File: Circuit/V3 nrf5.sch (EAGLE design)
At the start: 63 parts, among them J12 AMP FCI 10103594-0001LF, J7 CORTEX_DEBUG_SMD, Q1 BSS138, U1 AL8805, U2 MCP73831, U3 BC840M, U4 3.3V/150mA, U5 AL8805, U6 AL8805, U9 RICHTEK_TECHNOLOGY_CORPORATIO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

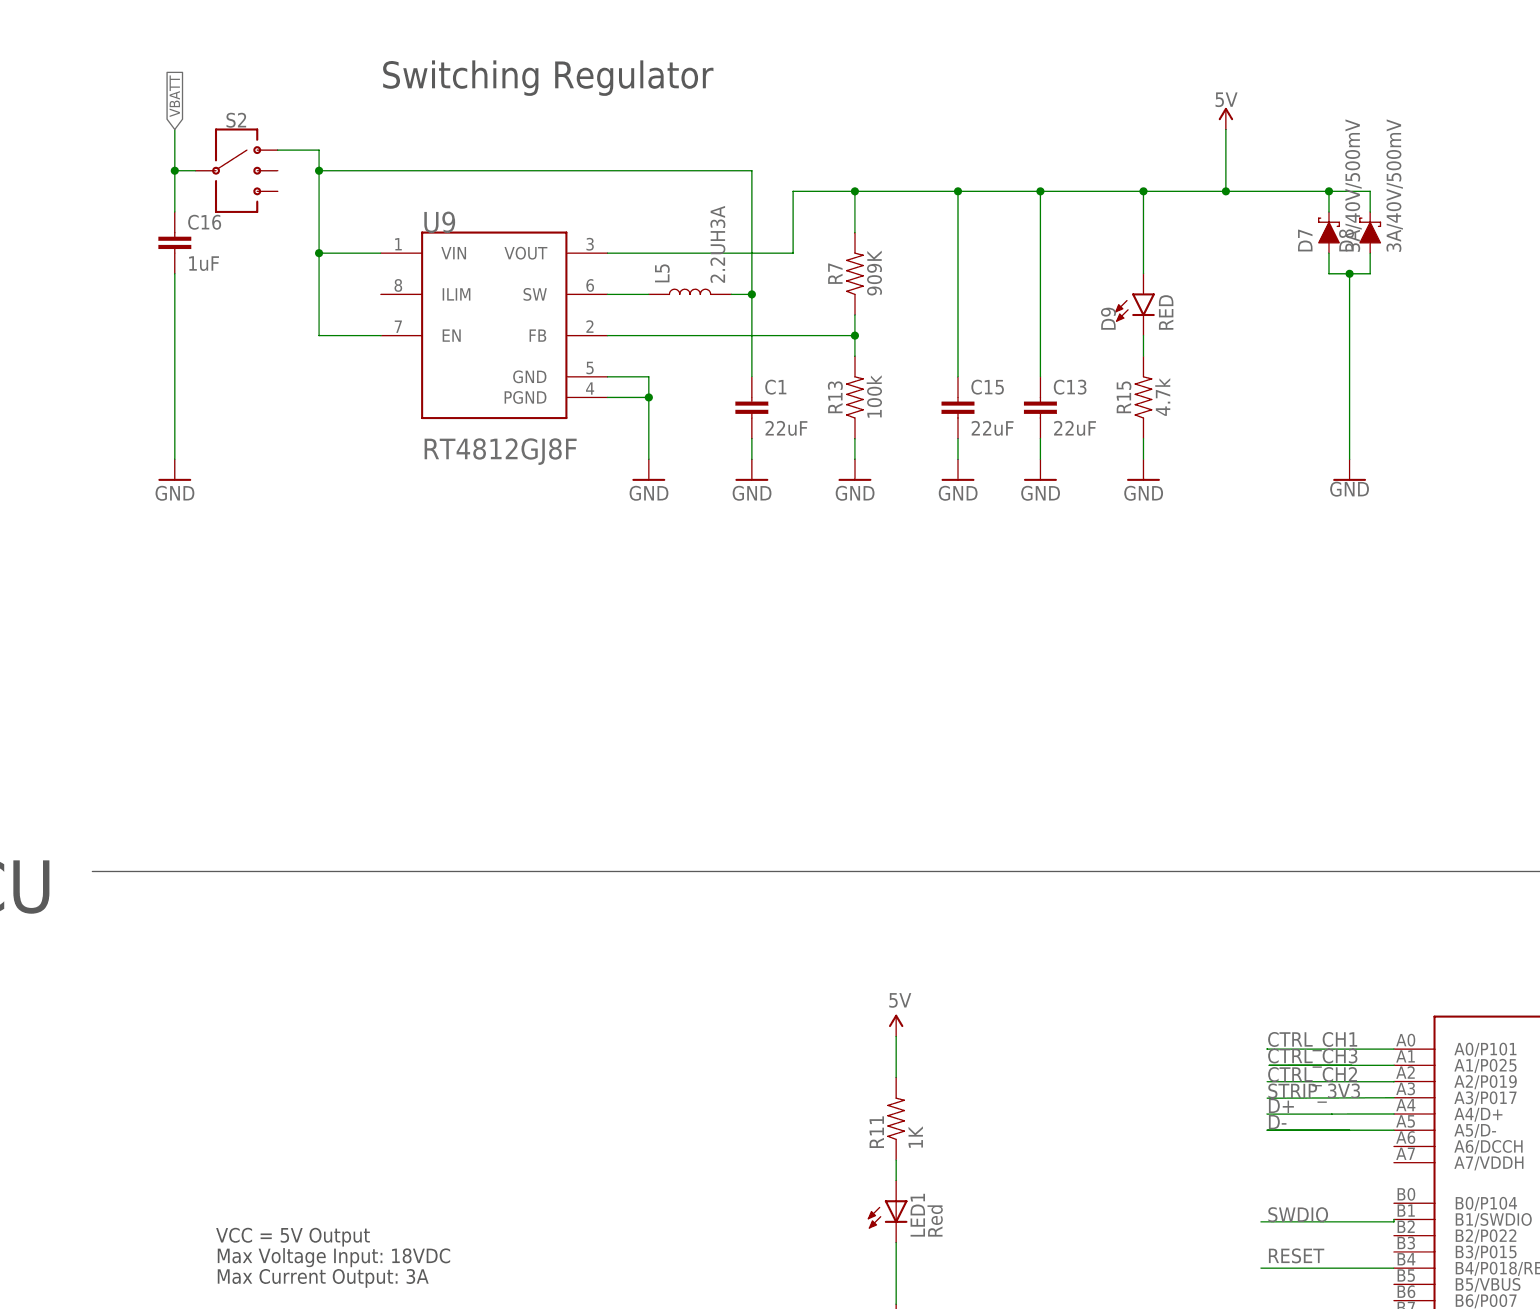
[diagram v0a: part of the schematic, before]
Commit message: Made changes after design review. Mostly adding digikey part numbers, switching out an inductor, and adding a pin to the bluetooth module.
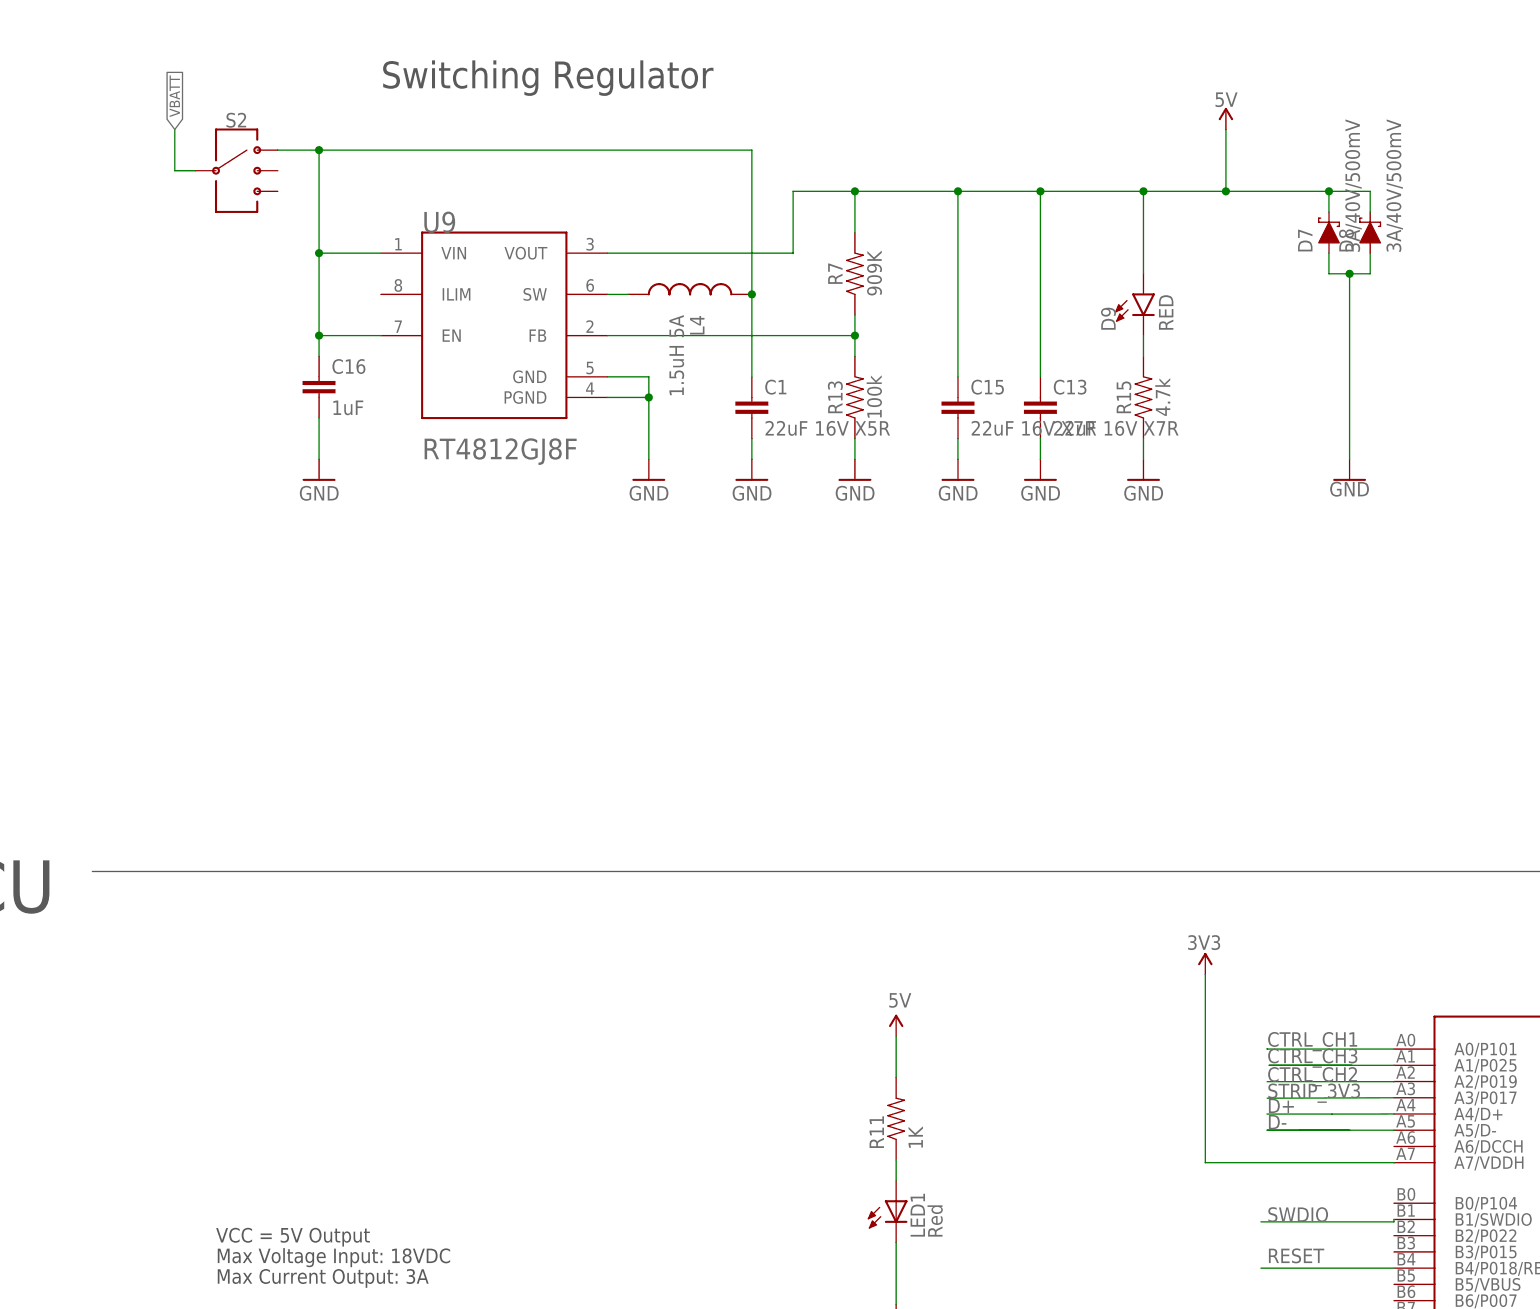
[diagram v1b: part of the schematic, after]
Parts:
- removed L5: 2.2UH3A, SparkFun-Coils:INDUCTOR-IFSC1515AHER2R2M01
- added L4: 1.5uH 5A, SparkFun-Passives:INDUCTORBOURNS_SRN6045
- C1: value 22uF -> 22uF 16V X5R; DIGIKEY (none) -> 1276-6780-2-ND
- C13, C15: value 22uF -> 22uF 16V X7R; DIGIKEY (none) -> 1276-6780-2-ND
- C16: DIGIKEY (none) -> 1276-6471-2-ND
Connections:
- removed net N$6: L5.1, U9.SW
- new net 3.3V: U3.A7/VDDH
- new net N$3: L4.1, U9.SW
- net VBATT: no longer C16.1
- net VBATT_ON: now also C16.1, L4.2; no longer L5.2
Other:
- moved on the sheet: C16
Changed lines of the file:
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@@
 <part name="D9" library="SparkFun-LED" deviceset="LED-RED" device="0603" value="RED"/>
 <part name="R15" library="SparkFun-Resistors" deviceset="4.7KOHM" device="-0603-1/10W-1%" value="4.7k"/>
-<part name="C13" library="SparkFun-Capacitors" deviceset="22UF" device="-0805-6.3V-20%" value="22uF"/>
-<part name="C15" library="SparkFun-Capacitors" deviceset="22UF" device="-0805-6.3V-20%" value="22uF"/>
-<part name="C16" library="SparkFun-Capacitors" deviceset="22UF" device="-0805-6.3V-20%" value="1uF"/>
+<part name="C13" library="SparkFun-Capacitors" deviceset="22UF" device="-0805-6.3V-20%" value="22uF 16V X7R">
+<attribute name="DIGIKEY" value="1276-6780-2-ND"/>
+</part>
+<part name="C15" library="SparkFun-Capacitors" deviceset="22UF" device="-0805-6.3V-20%" value="22uF 16V X7R">
+<attribute name="DIGIKEY" value="1276-6780-2-ND"/>
+</part>
+<part name="C16" library="SparkFun-Capacitors" deviceset="22UF" device="-0805-6.3V-20%" value="1uF">
+<attribute name="DIGIKEY" value="1276-6471-2-ND"/>
+</part>
 <part name="J12" library="con-molex-usb" deviceset="MICRO-USB-RECEPTACLE" device="47589-0001" value="AMP FCI 10103594-0001LF"/>
-<part name="L5" library="SparkFun-Coils" deviceset="INDUCTOR" device="-IFSC1515AHER2R2M01" value="2.2UH3A"/>
 <part name="U9" library="Richtek Technology Corporation - RT4812GJ8F" deviceset="RICHTEK_TECHNOLOGY_CORPORATION_RT4812GJ8F" device="RICHTEK_TECHNOLOGY_CORPORATION_RT4812GJ8F_0_0"/>
-<part name="C1" library="SparkFun-Capacitors" deviceset="22UF" device="-0805-6.3V-20%" value="22uF"/>
+<part name="C1" library="SparkFun-Capacitors" deviceset="22UF" device="-0805-6.3V-20%" value="22uF 16V X5R">
+<attribute name="DIGIKEY" value="1276-6780-2-ND"/>
+</part>
 <part name="GND12" library="SparkFun" deviceset="GND" device=""/>
 <part name="P+8" library="SparkFun-PowerSymbols" deviceset="VCC" device="" value="5V"/>
+<part name="P+9" library="SparkFun" deviceset="3.3V" device="" value="3V3"/>
+<part name="L4" library="SparkFun-Passives" deviceset="INDUCTOR" device="BOURNS_SRN6045" value="1.5uH 5A">
+<attribute name="DIGIKEY" value="587-2097-2-ND"/>
+</part>
 </parts>
 <sheets>
@@
 <attribute name="VALUE" x="142.24" y="332.74" size="1.778" layer="96"/>
 </instance>
-<instance part="GND19" gate="1" x="33.02" y="233.68" smashed="yes" rot="MR0">
-<attribute name="VALUE" x="35.56" y="231.14" size="1.778" layer="96" rot="MR0"/>
+<instance part="GND19" gate="1" x="50.8" y="233.68" smashed="yes" rot="MR0">
+<attribute name="VALUE" x="53.34" y="231.14" size="1.778" layer="96" rot="MR0"/>
 </instance>
 <instance part="R7" gate="G$1" x="116.84" y="259.08" smashed="yes" rot="R90">
@@
 <attribute name="NAME" x="141.224" y="244.221" size="1.778" layer="95" font="vector"/>
 <attribute name="VALUE" x="141.224" y="239.141" size="1.778" layer="96" font="vector"/>
+<attribute name="DIGIKEY" x="139.7" y="241.3" size="1.778" layer="96" display="off"/>
 </instance>
 <instance part="C15" gate="G$1" x="129.54" y="241.3" smashed="yes">
 <attribute name="NAME" x="131.064" y="244.221" size="1.778" layer="95" font="vector"/>
 <attribute name="VALUE" x="131.064" y="239.141" size="1.778" layer="96" font="vector"/>
-</instance>
-<instance part="C16" gate="G$1" x="33.02" y="261.62" smashed="yes">
-<attribute name="NAME" x="34.544" y="264.541" size="1.778" layer="95" font="vector"/>
-<attribute name="VALUE" x="34.544" y="259.461" size="1.778" layer="96" font="vector"/>
+<attribute name="DIGIKEY" x="129.54" y="241.3" size="1.778" layer="96" display="off"/>
+</instance>
+<instance part="C16" gate="G$1" x="50.8" y="243.84" smashed="yes">
+<attribute name="NAME" x="52.324" y="246.761" size="1.778" layer="95" font="vector"/>
+<attribute name="VALUE" x="52.324" y="241.681" size="1.778" layer="96" font="vector"/>
+<attribute name="DIGIKEY" x="50.8" y="243.84" size="1.778" layer="96" display="off"/>
 </instance>
 <instance part="J12" gate="G$1" x="93.98" y="337.82" smashed="yes" rot="MR0">
 <attribute name="NAME" x="96.52" y="345.44" size="1.778" layer="95" font="vector" rot="MR0"/>
-</instance>
-<instance part="L5" gate="G$1" x="96.52" y="256.54" smashed="yes" rot="R90">
-<attribute name="NAME" x="93.98" y="257.81" size="1.778" layer="95" font="vector" rot="R90"/>
-<attribute name="VALUE" x="99.06" y="257.81" size="1.778" layer="96" font="vector" rot="R90" align="top-left"/>
 </instance>
 <instance part="U9" gate="G$0" x="60.96" y="269.24" smashed="yes">
@@
 <attribute name="NAME" x="105.664" y="244.221" size="1.778" layer="95" font="vector"/>
 <attribute name="VALUE" x="105.664" y="239.141" size="1.778" layer="96" font="vector"/>
+<attribute name="DIGIKEY" x="104.14" y="241.3" size="1.778" layer="96" display="off"/>
 </instance>
 <instance part="GND12" gate="1" x="91.44" y="233.68" smashed="yes" rot="MR0">
@@
 <instance part="P+8" gate="G$1" x="30.48" y="106.68" smashed="yes">
 <attribute name="VALUE" x="30.48" y="109.474" size="1.778" layer="96" align="bottom-center"/>
+</instance>
+<instance part="P+9" gate="G$1" x="160.02" y="172.72" smashed="yes">
+<attribute name="VALUE" x="157.734" y="175.768" size="1.778" layer="96"/>
+</instance>
+<instance part="L4" gate="G$1" x="96.52" y="256.54" smashed="yes" rot="R90">
+<attribute name="NAME" x="96.52" y="254" size="1.778" layer="95" rot="R270"/>
+<attribute name="VALUE" x="93.98" y="254" size="1.778" layer="96" rot="R270"/>
+<attribute name="DIGIKEY" x="96.52" y="256.54" size="1.778" layer="96" rot="R90" display="off"/>
 </instance>
 </instances>
@@
 </segment>
 <segment>
-<pinref part="GND19" gate="1" pin="GND"/>
-<wire x1="33.02" y1="236.22" x2="33.02" y2="259.08" width="0.1524" layer="91"/>
-<pinref part="C16" gate="G$1" pin="2"/>
-</segment>
-<segment>
 <pinref part="R13" gate="G$1" pin="1"/>
 <pinref part="GND22" gate="1" pin="GND"/>
@@
 <wire x1="86.36" y1="243.84" x2="91.44" y2="243.84" width="0.1524" layer="91"/>
 <junction x="91.44" y="243.84"/>
+</segment>
+<segment>
+<pinref part="C16" gate="G$1" pin="2"/>
+<pinref part="GND19" gate="1" pin="GND"/>
+<wire x1="50.8" y1="241.3" x2="50.8" y2="236.22" width="0.1524" layer="91"/>
 </segment>
 </net>
@@
 </segment>
 <segment>
-<pinref part="C16" gate="G$1" pin="1"/>
-<wire x1="33.02" y1="266.7" x2="33.02" y2="271.78" width="0.1524" layer="91"/>
 <label x="33.02" y="276.86" size="1.27" layer="95" rot="R90" xref="yes"/>
 <pinref part="S2" gate="G$1" pin="3"/>
 <wire x1="33.02" y1="271.78" x2="33.02" y2="276.86" width="0.1524" layer="91"/>
 <wire x1="33.02" y1="271.78" x2="35.56" y2="271.78" width="0.1524" layer="91"/>
-<junction x="33.02" y="271.78"/>
 </segment>
 </net>
@@
 <pinref part="D2" gate="G$1" pin="A"/>
 <wire x1="124.46" y1="350.52" x2="127" y2="350.52" width="0.1524" layer="91"/>
-</segment>
-</net>
-<net name="N$6" class="0">
-<segment>
-<pinref part="L5" gate="G$1" pin="1"/>
-<pinref part="U9" gate="G$0" pin="SW"/>
-<wire x1="91.44" y1="256.54" x2="86.36" y2="256.54" width="0.1524" layer="91"/>
 </segment>
 </net>
@@
 <net name="VBATT_ON" class="0">
 <segment>
-<pinref part="C1" gate="G$1" pin="1"/>
-<pinref part="L5" gate="G$1" pin="2"/>
-<wire x1="104.14" y1="246.38" x2="104.14" y2="256.54" width="0.1524" layer="91"/>
-<wire x1="104.14" y1="256.54" x2="101.6" y2="256.54" width="0.1524" layer="91"/>
-<wire x1="104.14" y1="256.54" x2="104.14" y2="271.78" width="0.1524" layer="91"/>
-<wire x1="104.14" y1="271.78" x2="50.8" y2="271.78" width="0.1524" layer="91"/>
-<junction x="104.14" y="256.54"/>
 <pinref part="U9" gate="G$0" pin="VIN"/>
 <wire x1="50.8" y1="261.62" x2="58.42" y2="261.62" width="0.1524" layer="91"/>
-<wire x1="50.8" y1="261.62" x2="50.8" y2="271.78" width="0.1524" layer="91"/>
 <pinref part="U9" gate="G$0" pin="EN"/>
 <wire x1="58.42" y1="251.46" x2="50.8" y2="251.46" width="0.1524" layer="91"/>
 <wire x1="50.8" y1="251.46" x2="50.8" y2="261.62" width="0.1524" layer="91"/>
+<pinref part="S2" gate="G$1" pin="1"/>
+<wire x1="104.14" y1="246.38" x2="104.14" y2="256.54" width="0.1524" layer="91"/>
+<pinref part="C1" gate="G$1" pin="1"/>
+<wire x1="104.14" y1="256.54" x2="104.14" y2="274.32" width="0.1524" layer="91"/>
+<wire x1="45.72" y1="274.32" x2="50.8" y2="274.32" width="0.1524" layer="91"/>
+<wire x1="50.8" y1="274.32" x2="104.14" y2="274.32" width="0.1524" layer="91"/>
+<wire x1="50.8" y1="261.62" x2="50.8" y2="274.32" width="0.1524" layer="91"/>
 <junction x="50.8" y="261.62"/>
-<pinref part="S2" gate="G$1" pin="1"/>
-<wire x1="45.72" y1="274.32" x2="50.8" y2="274.32" width="0.1524" layer="91"/>
-<wire x1="50.8" y1="274.32" x2="50.8" y2="271.78" width="0.1524" layer="91"/>
-<junction x="50.8" y="271.78"/>
-</segment>
-</net>
+<junction x="50.8" y="274.32"/>
+<pinref part="C16" gate="G$1" pin="1"/>
+<wire x1="50.8" y1="251.46" x2="50.8" y2="248.92" width="0.1524" layer="91"/>
+<junction x="50.8" y="251.46"/>
+<pinref part="L4" gate="G$1" pin="2"/>
+<junction x="104.14" y="256.54"/>
+</segment>
+</net>
+<net name="3.3V" class="0">
+<segment>
+<pinref part="U3" gate="G$1" pin="A7/VDDH"/>
+<pinref part="P+9" gate="G$1" pin="3.3V"/>
+<wire x1="183.266" y1="149.534" x2="160.02" y2="149.534" width="0.1524" layer="91"/>
+<wire x1="160.02" y1="149.534" x2="160.02" y2="172.72" width="0.1524" layer="91"/>
+</segment>
+</net>
+<net name="N$3" class="0">
+<segment>
+<pinref part="L4" gate="G$1" pin="1"/>
+<pinref part="U9" gate="G$0" pin="SW"/>
+<wire x1="88.9" y1="256.54" x2="86.36" y2="256.54" width="0.1524" layer="91"/>
+</segment>
+</net>

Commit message: Replacing 3V3 -> 5V booster footprint, relaying out with datasheet recommendations. Still need to swap screw terminals for JST connectors on high current LEDs, find a better micro USB connector (with proper footprint), and find a slide switch.
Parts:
- removed C1: 22uF 16V X5R, SparkFun-Capacitors:22UF-0805-6.3V-20%
- removed U9: RICHTEK_TECHNOLOGY_CORPORATION_RT4812GJ8FRICHTEK_TECHNOLOGY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, Richtek Technology Corporation - RT4812GJ8F:RICHTEK_TECHNOLOGY_CORPORATION_RT4812GJ8FRICHTEK_TECHNOLOGY_CORPORATION_RT4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
- added U7: MP3414AGJ-Z, MP3414AGJ-Z:MP3414AGJ-Z
- C15: value 22uF 16V X7R -> 1uF 16V X7R
- C16: value 1uF -> 22uF
- R13: value 100k -> 110k
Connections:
- net 5V: now also U7.OUT; no longer U9.VOUT
- net GND: now also U7.AGND, U7.PGND; no longer C1.2, U9.GND, U9.PGND
- net N$3: now also U7.SW; no longer U9.SW
- net N$9: now also U7.FB; no longer U9.FB
- net VBATT_ON: now also U7.EN, U7.IN; no longer C1.1, U9.EN, U9.VIN
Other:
- note added: "3V3 LDO"
- note added: "Output capacity: 5V, 3A"
- note added: "POWER"
- note added: "Switching Boost Regulator"
- note added: "VBATT in is 3.7V, boosted to OUT 5V, 3A max"
- note removed: "Charger"
- note removed: "For heavy duty use: Use 2A switch in switch bypass pins, or jump with wire."
- note removed: "Output capacity: 5V, 1A for 3.0V to 4.2V battery voltage."
- note removed: "Switching Regulator"
- moved on the sheet: C10, C11, C12, C13, C15, C16, C9, D1, D2, D3, D7, D8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

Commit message: Switching USB micro footprint to match the digikey component. Also switching out JSTs for 2-pin screw terminals on high current LEDs. We'll see how reliable those are, may need to switch to a latching mechanism. Board is ready to print!
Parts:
- removed J12: AMP FCI 10103594-0001LF, con-molex-usb:MICRO-USB-RECEPTACLE47589-0001
- removed JP1, JP2, JP4: (no value), SparkFun-Connectors:CONN_02
- removed S2: (no value), SparkFun-Switches:SWITCH-SP3T-SMD
- added J4: USB Micro, 2040002-1:2040002-1
- added S3: (no value), SparkFun-Switches:SWITCH-SPDT-SMD-RIGHT-ANGLE
- J1, J2, J3: device SparkFun-Connectors:JST_2MM_MALE -> SparkFun-Connectors:CONN_023.5MM
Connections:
- net 5VIN: now also J4.VBUS; no longer J12.1
- net GND: now also J4.GND; no longer J12.5
- net OUT1+: now also J1.2; no longer J1.+, JP4.1
- net OUT1-: now also J1.1; no longer J1.-, JP4.2
- net OUT2+: now also J2.2; no longer J2.+, JP1.1
- net OUT2-: now also J2.1; no longer J2.-, JP1.2
- net OUT3+: now also J3.2; no longer J3.+, JP2.1
- net OUT3-: now also J3.1; no longer J3.-, JP2.2
- net VBATT: now also S3.P; no longer S2.3
- net VBATT_ON: now also S3.S; no longer S2.1
